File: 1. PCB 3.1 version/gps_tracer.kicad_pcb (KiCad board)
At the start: 2 copper layers, 65 x 38.2 mm, 98 parts, among them IC1 TC4056A, J1 Mic, J2 SPK, J3 I2C, J4 BATTERY, J5 Micro_SD_Card, P1 USB_C_Plug_USB2.0, Q1 S8050, Q2 S8050, Q3 FDN358P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

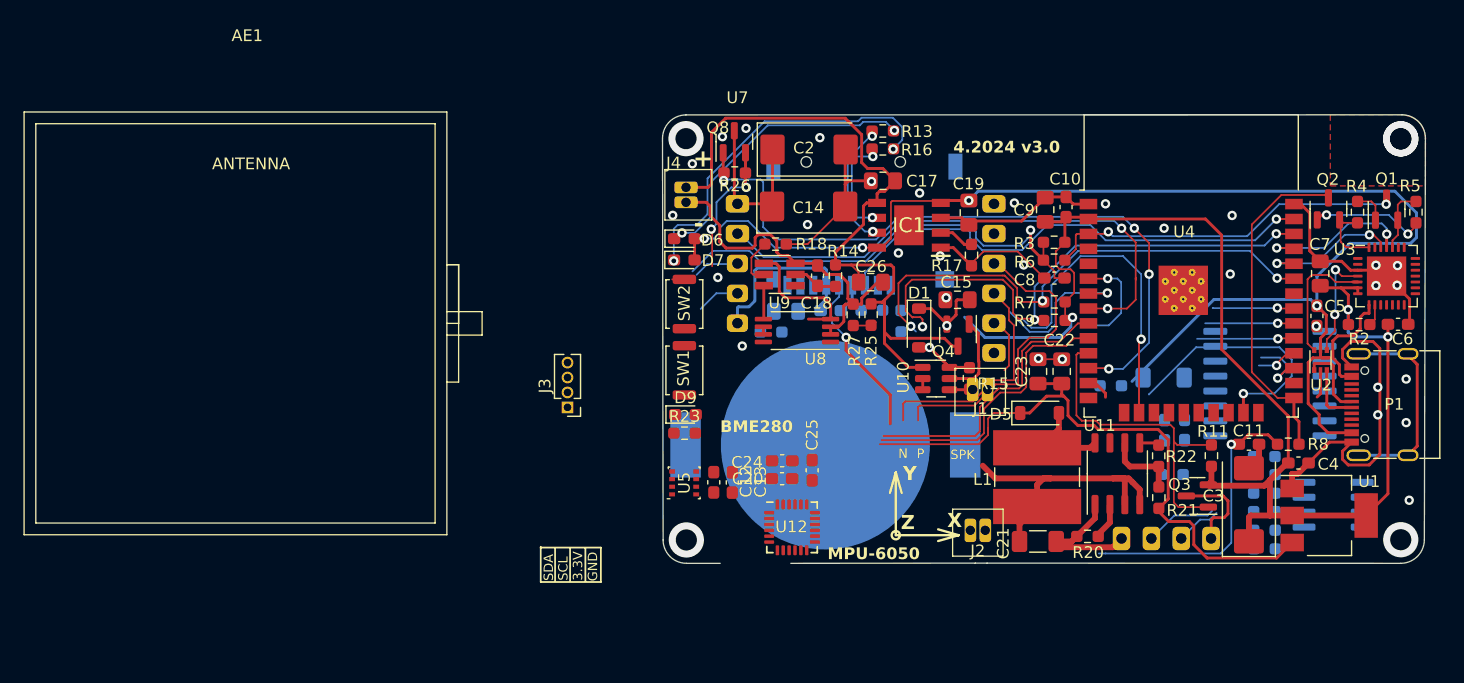
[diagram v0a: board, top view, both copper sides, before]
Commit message: finiched work with GPS loging into file
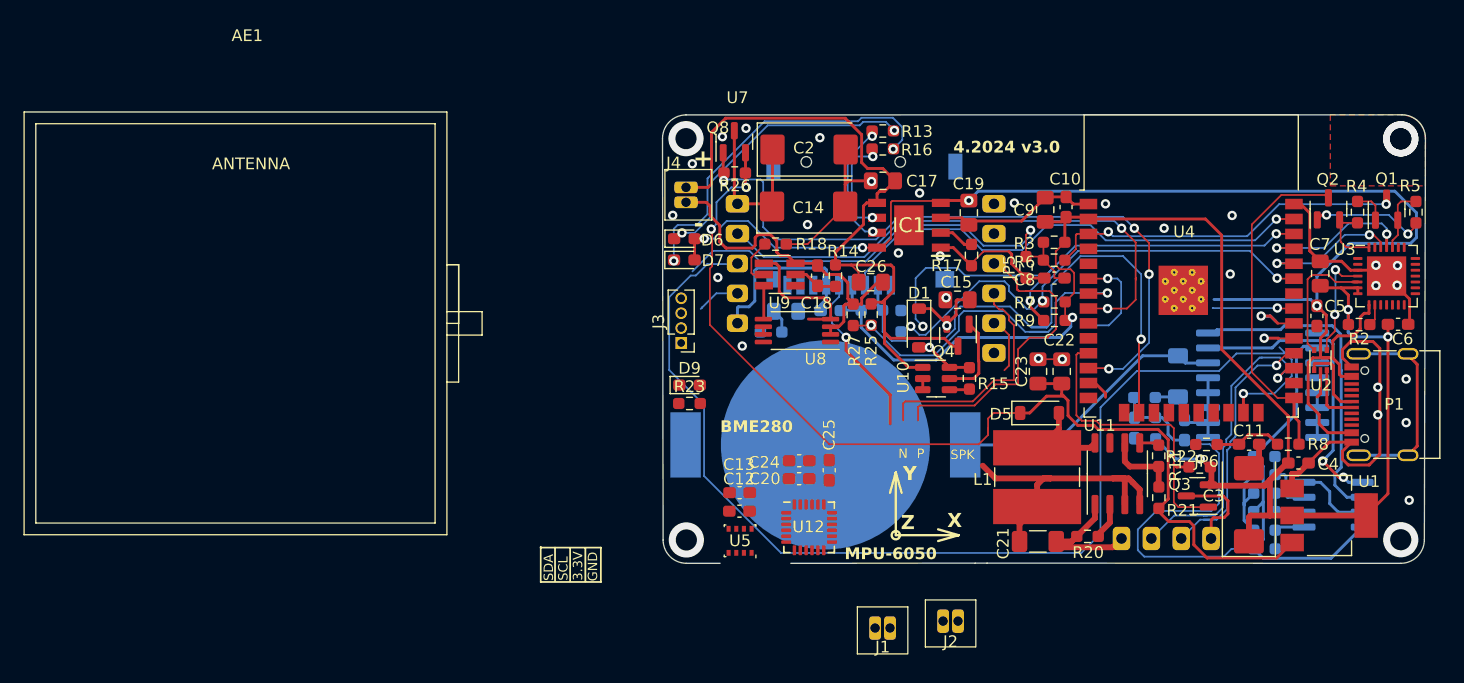
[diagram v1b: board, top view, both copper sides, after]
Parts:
- removed SW1: EN, Button_Switch_SMD:SW_Push_SPST_NO_Alps_SKRK
- removed SW2: BOOT, Button_Switch_SMD:SW_Push_SPST_NO_Alps_SKRK
- added JP5: EN, Resistor_SMD:R_0603_1608Metric_Pad0.98x0.95mm_HandSolder, F.Cu at (79.2, 50.0)
- added JP6: BOOT, Resistor_SMD:R_0603_1608Metric_Pad0.98x0.95mm_HandSolder, F.Cu at (94.6, 65.1)
- moved J1 21.9 mm to (68.9, 80.7)
- moved J3 11.1 mm to (49.8, 56.4)
- moved J2 8.07 mm to (74.7, 80.1)
- moved U5 6.86 mm to (54.8, 73.3), turned to 180 degrees
- moved JP4 4.20 mm to (90.2, 63.7), turned to -90 degrees
- moved C12 3.29 mm to (54.8, 70.8), turned to 0 degrees
- moved R31 3.05 mm to (89.3, 61.1)
- moved C28 2.57 mm to (88.4, 63.7), turned to -90 degrees
- moved R23 2.56 mm to (50.5, 61.6)
- moved D9 2.53 mm to (50.5, 60.0)
- moved C20 1.45 mm to (59.9, 68.0)
- moved C25 1.45 mm to (62.4, 67.3)
- moved C24 1.45 mm to (59.9, 66.5)
- moved U12 1.45 mm to (60.7, 72.1)
- moved R11 1.39 mm to (94.0, 67.0), turned to 0 degrees
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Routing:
- net RXD_GSM: track 25.9 -> 98.4 mm
- net Net-(JP4-A): track 0.00 -> 68.3 mm
- net +3.3V: track 115.8 -> 142.3 mm, vias 3 -> 4
- net SCL: track 46.1 -> 72.5 mm
- net unconnected-(U4-IO33-Pad9): track 24.6 -> 0.00 mm
- net unconnected-(U4-IO25-Pad10): track 24.4 -> 0.00 mm
- net Net-(BT1-+): track 0.00 -> 24.1 mm
- net GND: track 123.0 -> 146.8 mm, vias 31 -> 29
- net GSM_POWER_SOURSE: track 65.7 -> 89.4 mm
- net MICROSD_CS: track 33.6 -> 53.9 mm
- net SDA: track 45.2 -> 65.3 mm, vias 3 -> 5
- net Net-(JP6-A): track 24.0 -> 5.83 mm, vias 1 -> 0
- net BATTERY_VOLTAGE: track 15.4 -> 31.9 mm, vias 1 -> 2
- net GPS_TX: track 11.8 -> 27.5 mm
- net GPS_RX: track 7.50 -> 22.6 mm
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
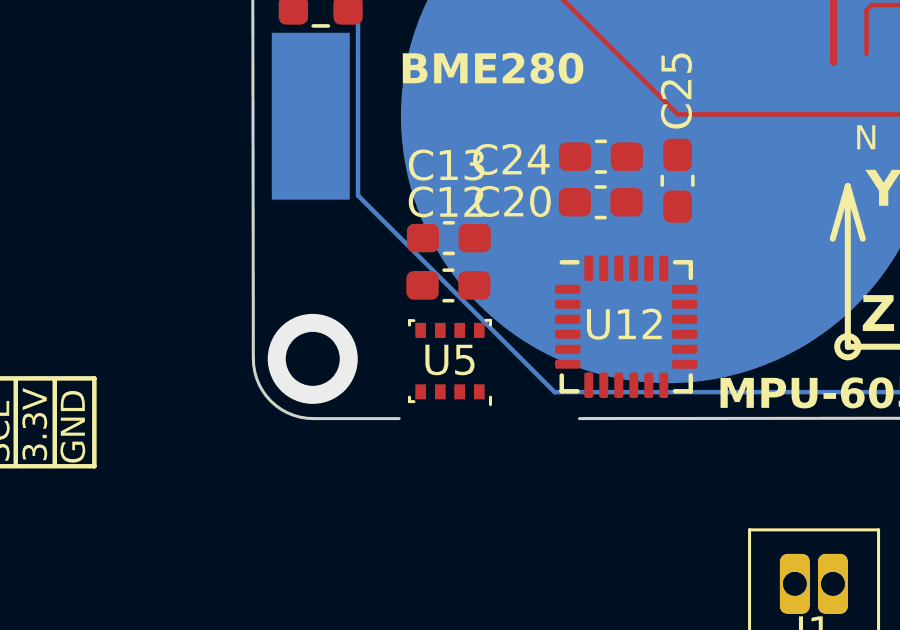
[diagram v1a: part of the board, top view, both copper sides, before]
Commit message: SIM800l receive and send sms, and answer on call my number
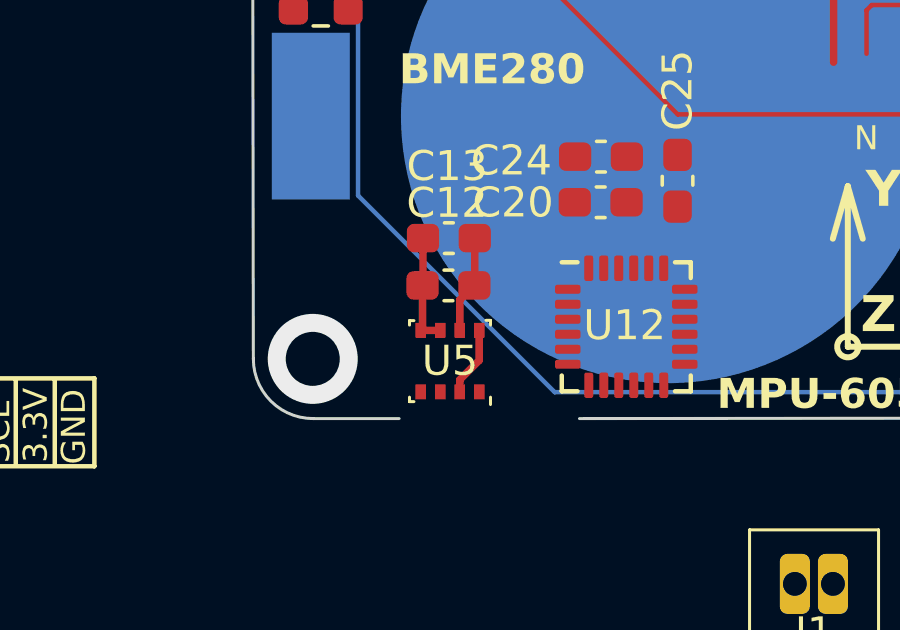
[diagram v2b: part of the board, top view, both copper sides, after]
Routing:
- net +3.3V: track 142.3 -> 148.4 mm
- net GND: track 146.8 -> 150.1 mm
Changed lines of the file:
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@@
   (segment (start 111.85 54.6216) (end 111.7854 54.6862) (width 0.25) (layer "F.Cu") (net 2))
   (segment (start 104.267 60.743) (end 103.98 61.03) (width 0.25) (layer "F.Cu") (net 2))
+  (segment (start 55.17 72.25) (end 55.17 71.2368) (width 0.25) (layer "F.Cu") (net 2))
   (segment (start 63.7931 44.8056) (end 63.7931 42.92) (width 0.25) (layer "F.Cu") (net 2))
   (segment (start 88.8746 64.939) (end 90.304 64.939) (width 0.25) (layer "F.Cu") (net 2))
@@
   (segment (start 63.7931 42.92) (end 63.7931 39.9933) (width 0.25) (layer "F.Cu") (net 2))
   (segment (start 109.3942 50.2332) (end 109.8942 50.7332) (width 0.25) (layer "F.Cu") (net 2))
+  (segment (start 55.17 71.2368) (end 55.6556 70.7512) (width 0.25) (layer "F.Cu") (net 2))
+  (segment (start 55.67 70.7368) (end 55.6556 70.7512) (width 0.25) (layer "F.Cu") (net 2))
   (segment (start 74.55 49.654761) (end 74.55 49.8564) (width 0.15) (layer "F.Cu") (net 2))
   (segment (start 87.3252 73.0758) (end 86.578 73.823) (width 0.5) (layer "F.Cu") (net 2))
@@
   (segment (start 79.19 50.9) (end 77.97 49.68) (width 0.25) (layer "F.Cu") (net 2))
   (segment (start 99.0346 65.0494) (end 99.0346 66.2295) (width 0.5) (layer "F.Cu") (net 2))
+  (segment (start 55.67 69.175) (end 55.67 70.7368) (width 0.25) (layer "F.Cu") (net 2))
   (segment (start 64.0919 42.6212) (end 63.7931 42.92) (width 0.25) (layer "F.Cu") (net 2))
   (segment (start 108.409126 66.8162) (end 106.625674 66.8162) (width 0.25) (layer "F.Cu") (net 2))
@@
   (segment (start 99.96 71.12) (end 101.8536 71.12) (width 0.5) (layer "F.Cu") (net 3))
   (segment (start 106.02 51.7332) (end 107.4442 51.7332) (width 0.25) (layer "F.Cu") (net 3))
+  (segment (start 55.17 73.9) (end 55.17 74.3) (width 0.25) (layer "F.Cu") (net 3))
   (segment (start 107.4442 51.7332) (end 107.4442 52.2332) (width 0.25) (layer "F.Cu") (net 3))
+  (segment (start 53.87 72.25) (end 54.52 72.25) (width 0.25) (layer "F.Cu") (net 3))
   (segment (start 101.526 66.6496) (end 101.416949 66.6496) (width 0.5) (layer "F.Cu") (net 3))
   (segment (start 99.485949 68.5806) (end 99.96 68.106549) (width 0.5) (layer "F.Cu") (net 3))
@@
   (segment (start 80.8228 46.1186) (end 82.2 46.1186) (width 0.25) (layer "F.Cu") (net 3))
   (segment (start 98.171 73.3181) (end 98.171 71.269) (width 0.5) (layer "F.Cu") (net 3))
+  (segment (start 53.9306 72.1894) (end 53.87 72.25) (width 0.25) (layer "F.Cu") (net 3))
   (segment (start 94.7166 68.5038) (end 94.7934 68.5806) (width 0.5) (layer "F.Cu") (net 3))
   (segment (start 82.4992 47.8536) (end 82.4992 45.8194) (width 0.25) (layer "F.Cu") (net 3))
@@
   (segment (start 80.7742 46.07) (end 80.8228 46.1186) (width 0.25) (layer "F.Cu") (net 3))
   (segment (start 82.983498 50.149014) (end 82.05833 50.149014) (width 0.15) (layer "F.Cu") (net 3))
+  (segment (start 53.945 69.175) (end 53.945 70.7368) (width 0.25) (layer "F.Cu") (net 3))
   (segment (start 95.85 56.98) (end 101.526 62.656) (width 0.25) (layer "F.Cu") (net 3))
   (segment (start 98.32 71.12) (end 99.96 71.12) (width 0.5) (layer "F.Cu") (net 3))
   (segment (start 95.85 47.25) (end 95.85 56.98) (width 0.25) (layer "F.Cu") (net 3))
   (segment (start 104.4206 51.7332) (end 106.02 51.7332) (width 0.25) (layer "F.Cu") (net 3))
+  (segment (start 55.82 72.25) (end 55.82 73.25) (width 0.25) (layer "F.Cu") (net 3))
   (segment (start 84.3518 45.7178) (end 84.5064 45.8724) (width 0.25) (layer "F.Cu") (net 3))
+  (segment (start 53.945 70.7368) (end 53.9306 70.7512) (width 0.25) (layer "F.Cu") (net 3))
   (segment (start 94.98 68.2404) (end 94.7166 68.5038) (width 0.5) (layer "F.Cu") (net 3))
   (segment (start 94.98 66.935) (end 94.98 68.2404) (width 0.5) (layer "F.Cu") (net 3))
@@
   (segment (start 98.171 71.269) (end 98.32 71.12) (width 0.5) (layer "F.Cu") (net 3))
   (segment (start 81.73 48.6228) (end 82.4992 47.8536) (width 0.15) (layer "F.Cu") (net 3))
+  (segment (start 53.9306 70.7512) (end 53.9306 72.1894) (width 0.25) (layer "F.Cu") (net 3))
   (segment (start 94.713469 66.99) (end 94.025337 66.301868) (width 0.15) (layer "F.Cu") (net 3))
+  (segment (start 55.82 73.25) (end 55.17 73.9) (width 0.25) (layer "F.Cu") (net 3))
   (segment (start 106.64 52.3532) (end 106.02 51.7332) (width 0.25) (layer "F.Cu") (net 3))
   (segment (start 106.64 54.86) (end 106.64 52.3532) (width 0.25) (layer "F.Cu") (net 3))

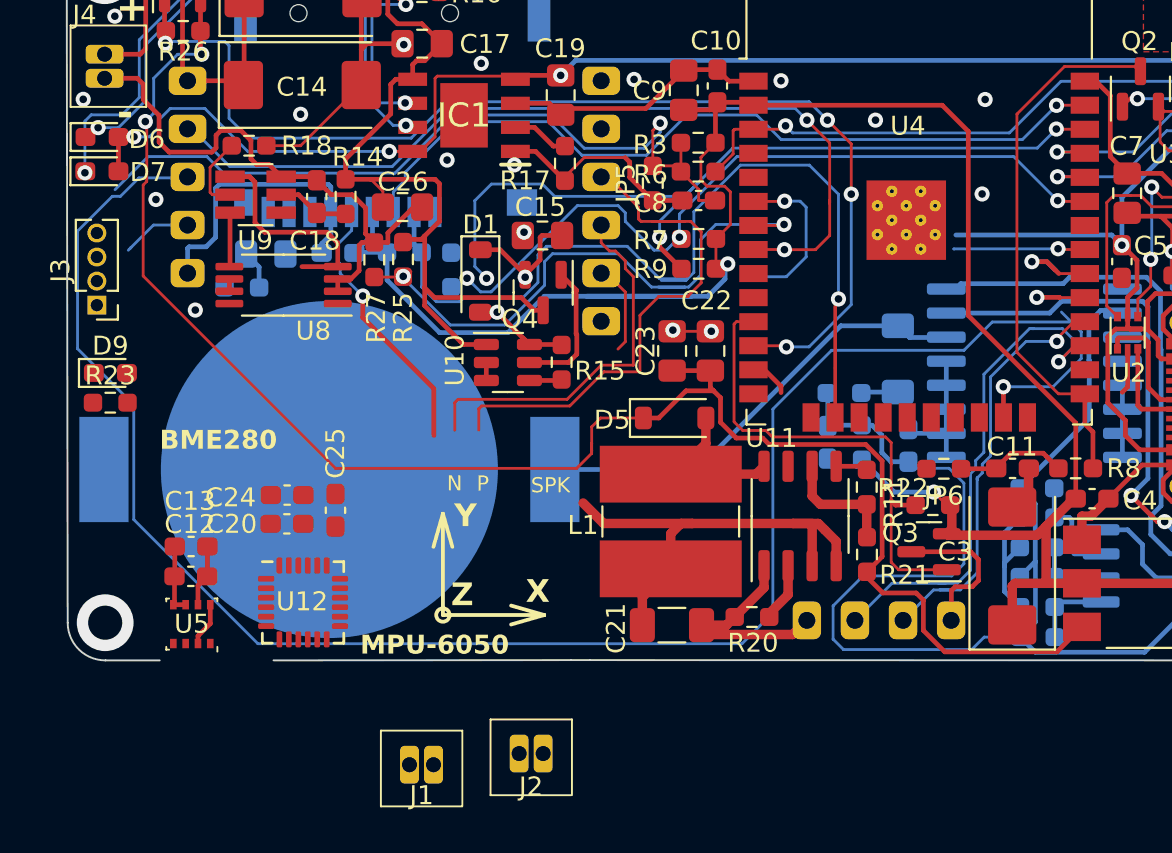
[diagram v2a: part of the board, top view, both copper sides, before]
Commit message: BUG with SMS was fixed
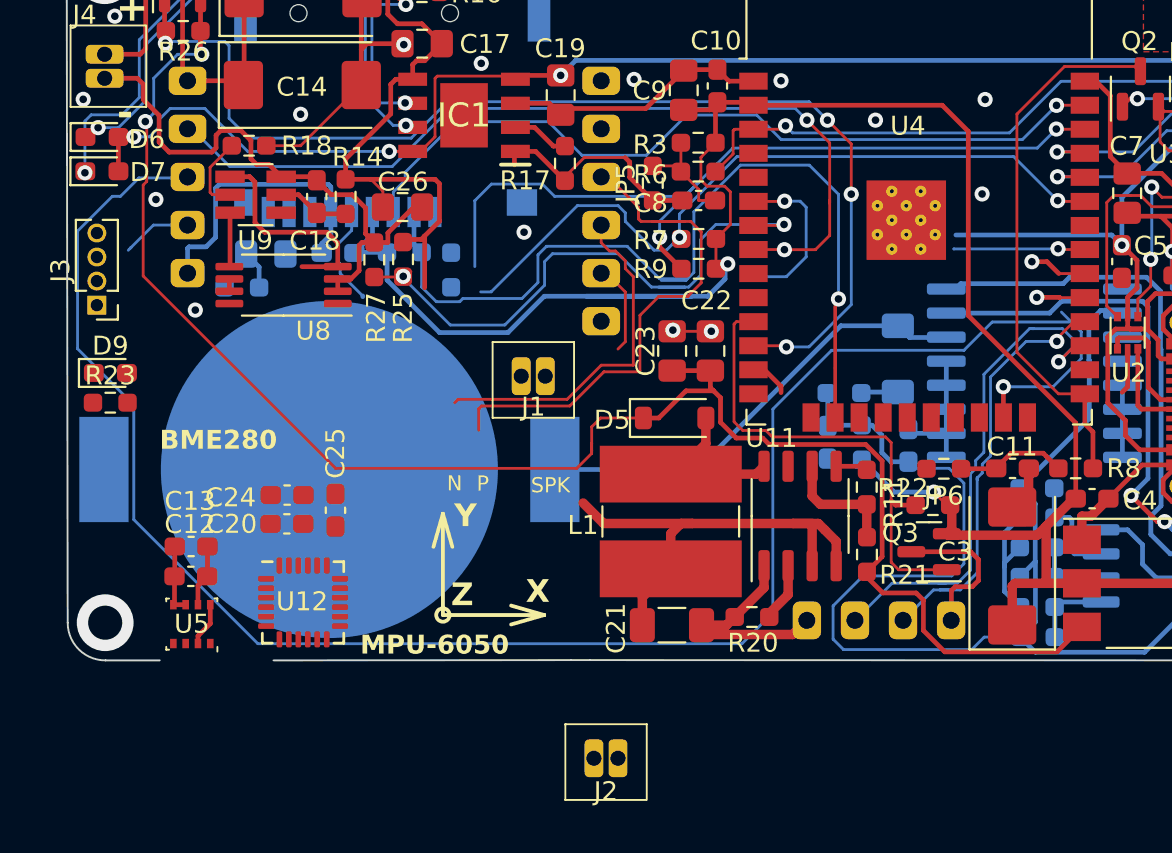
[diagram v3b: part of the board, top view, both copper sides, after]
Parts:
- removed C15: 22u, Capacitor_SMD:C_0805_2012Metric_Pad1.18x1.45mm_HandSolder
- removed D1: BAT48ZFILM, Diode_SMD:D_SOD-123
- removed Q4: LTC4412, Package_TO_SOT_SMD:SOT-23
- removed R15: 470k, Resistor_SMD:R_0603_1608Metric_Pad0.98x0.95mm_HandSolder
- removed U10: LTC4412xS6, Package_TO_SOT_SMD:TSOT-23-6
- moved J1 21.4 mm to (74.8, 60.2)
- moved J2 3.96 mm to (78.6, 80.4)
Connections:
- C21 pad 1: Net-(D1-K) -> Net-(IC1-BAT)
- L1 pad 1: Net-(D1-K) -> Net-(IC1-BAT)
- U11 pad 3: Net-(D1-K) -> Net-(IC1-BAT)
- U11 pad 4: Net-(D1-K) -> Net-(IC1-BAT)
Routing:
- net Net-(JP5-B): track 41.0 -> 5.91 mm, vias 1 -> 0
- net Net-(D1-K): track 32.4 -> 0.00 mm, vias 1 -> 0
- net Net-(IC1-BAT): track 62.1 -> 75.9 mm
- net MICROSD_CLK: track 16.2 -> 7.32 mm, vias 1 -> 0
- net Net-(Q4-G): track 7.24 -> 0.00 mm
- net +5V: track 124.9 -> 119.4 mm, vias 5 -> 4
- net Net-(U10-STAT): track 1.72 -> 0.00 mm
- net RED_LED: track 4.51 -> 3.06 mm
- net Net-(J1-Pin_1): track 20.0 -> 18.5 mm
- net SCL: track 72.5 -> 71.2 mm, vias 3 -> 2
- net SDA: track 65.3 -> 64.3 mm, vias 5 -> 4
- net GND: track 150.1 -> 149.1 mm, vias 29 -> 27
